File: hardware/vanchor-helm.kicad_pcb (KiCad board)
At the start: 2 copper layers, 200 x 150 mm, 113 parts, among them J1 PI_40PIN_STACK, J10 DISP PWR 5V, J11 AS5600, J12 PICO UTIL, J16 LOGIC 12-48V, J17 12V_LINK, J18 LUG BATT+, J19 LUG MOTOR A, J2 PI_BREAKOUT, J20 LUG MOTOR B, J21 LUG GND, J22 SERVO MOTOR, J3 UART0 ttyAMA0, J4 UART2 ttyAMA2, J5 UART3 ttyAMA3, J6 UART4 ttyAMA4, J7 UART5 ttyAMA5, J8 I2C1 spare, J9 FAN 5V, Q1 IRF9540N, Q10 IRF100P219, Q3 IRF100P219, Q4 IRF100P219, Q5 IRF100P219, Q6 IRF100P219, Q7 IRF100P219, Q8 IRF100P219, Q9 IRF100P219, U1 Pico 2, U10 ACS758LCB-100B, U5 D36V50F5, U6 D36V50F12, U7 BTN8982TA, U8 BTN8982TA, U9 HIP4082IPZ

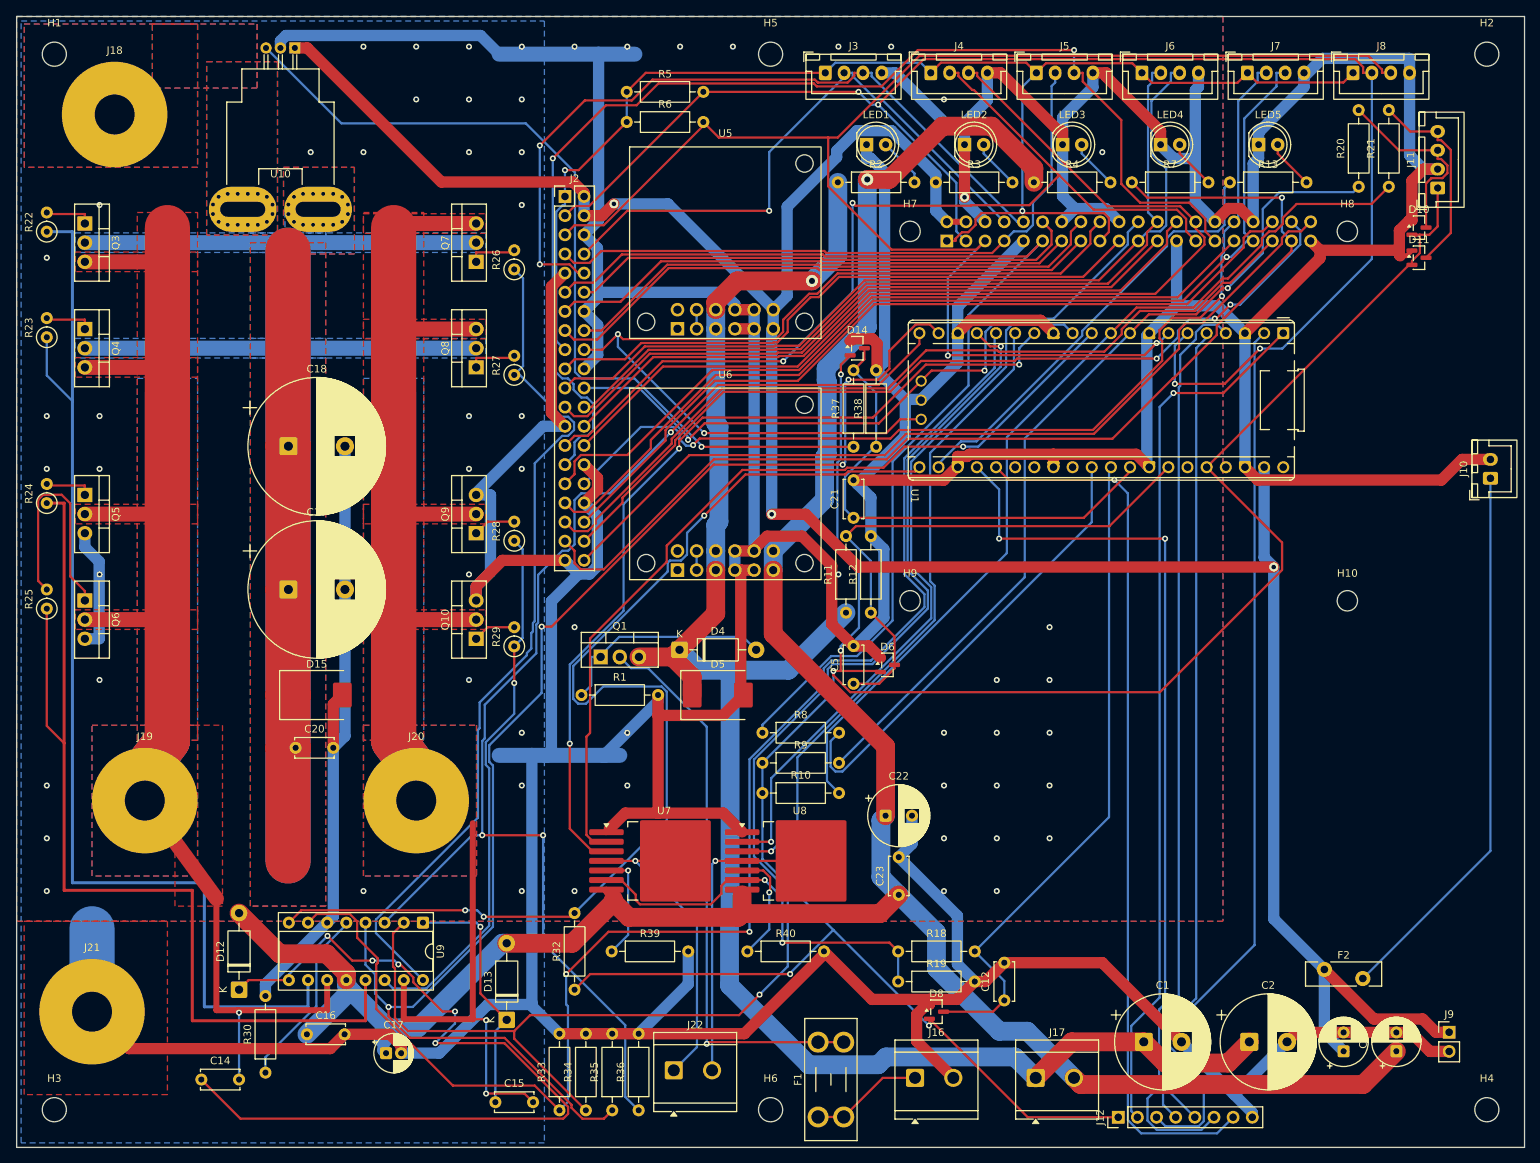
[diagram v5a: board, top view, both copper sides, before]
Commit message: cost passes 5-9: audits + cost-driver analysis + variant notes (docs/cost-optimization-log.md); v3 board script 150x120
Co-Authored-By: Claude Fable 5 <noreply@anthropic.com>
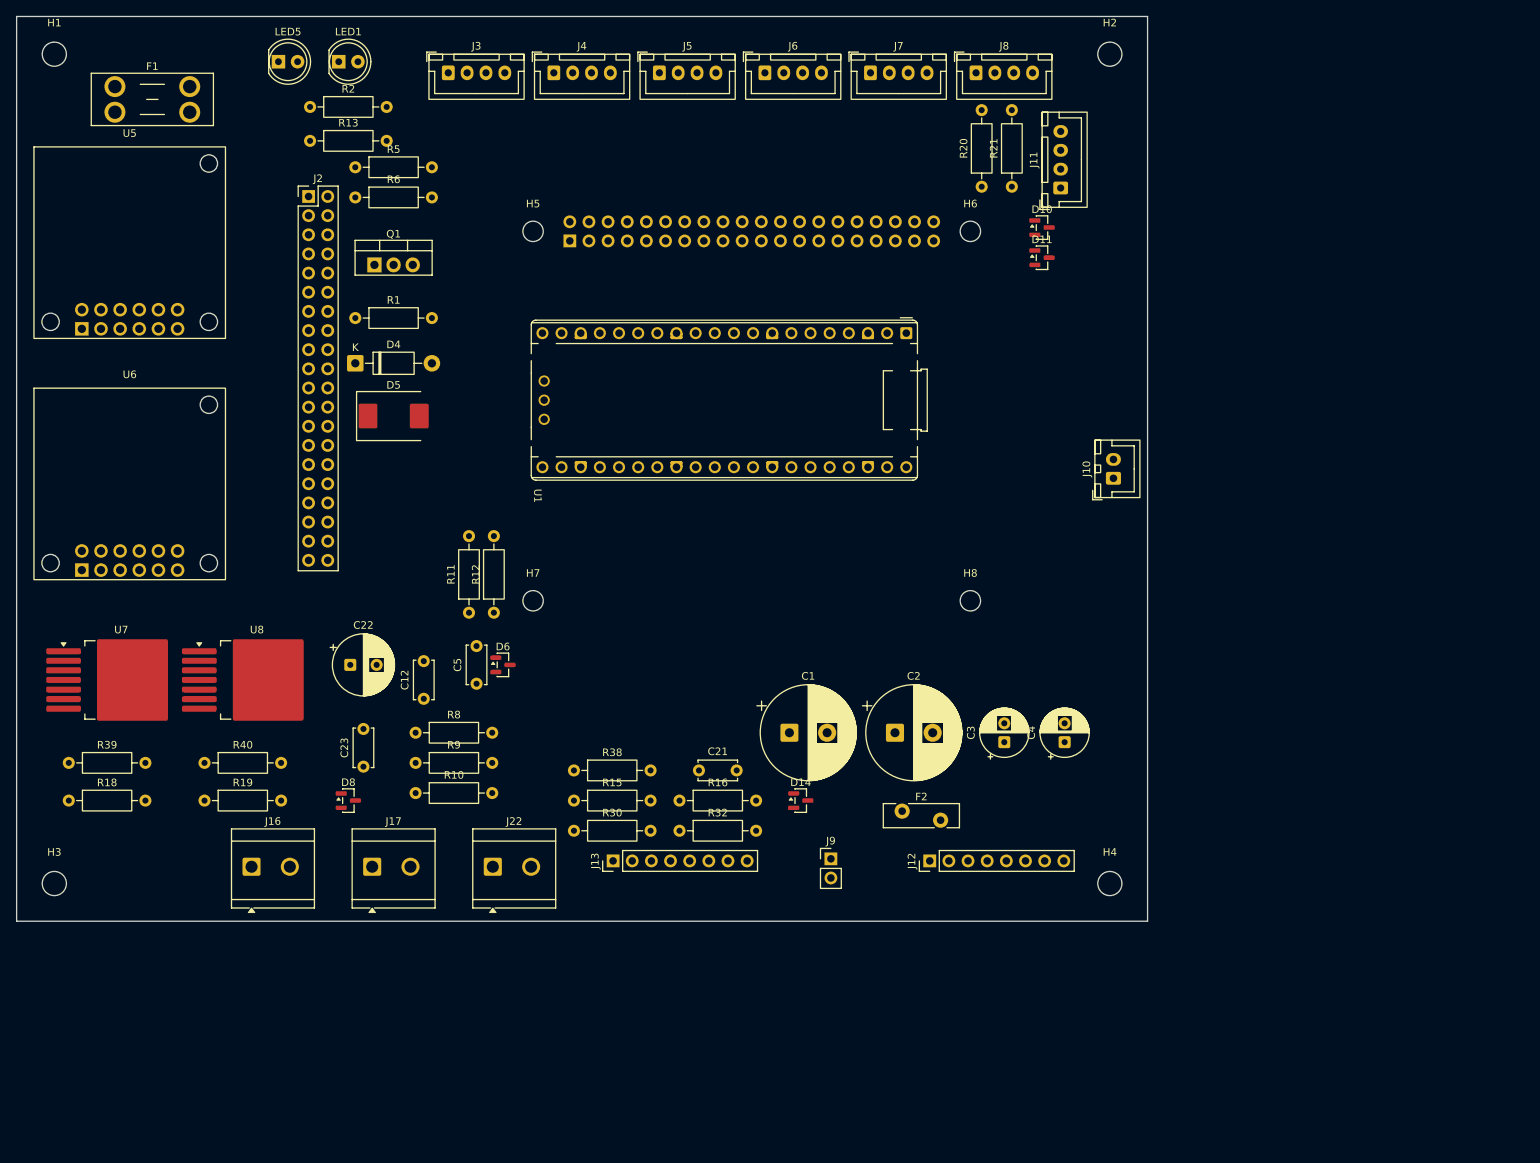
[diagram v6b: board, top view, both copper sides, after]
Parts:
- removed C14, C15: 1u/50V, C_Disc_D5.0mm_W2.5mm_P5.00mm
- removed C16: 100n, C_Disc_D5.0mm_W2.5mm_P5.00mm
- removed C17: 10u/25V, CP_Radial_D5.0mm_P2.00mm
- removed C18, C19: 2200u/63V, CP_Radial_D18.0mm_P7.50mm
- removed C20: 1u/100V film, C_Disc_D5.0mm_W2.5mm_P5.00mm
- removed D12, D13: UF4007, D_DO-41_SOD81_P10.16mm_Horizontal
- removed D15: SMCJ58A, D_SMC
- removed H10, H9: MountingHole_2.7mm_M2.5, MountingHole_2.7mm_M2.5
- removed J18: LUG BATT+, Lug_M5
- removed J19: LUG MOTOR A, Lug_M5
- removed J20: LUG MOTOR B, Lug_M5
- removed J21: LUG GND, Lug_M5
- removed LED2, LED3, LED4: green, LED_D5.0mm
- removed Q10, Q3, Q4, Q5, Q6, Q7, Q8, Q9: IRF100P219, TO-220-3_Vertical
- removed R22, R23, R24, R25, R26, R27, R28, R29: 10R, R_Axial_DIN0207_L6.3mm_D2.5mm_P2.54mm_Vertical
- removed R3, R7: 1k, R_Axial_DIN0207_L6.3mm_D2.5mm_P10.16mm_Horizontal
- removed R33, R34, R35, R36: 100k, R_Axial_DIN0207_L6.3mm_D2.5mm_P10.16mm_Horizontal
- removed R37: 10k, R_Axial_DIN0207_L6.3mm_D2.5mm_P10.16mm_Horizontal
- removed R4: 4.7k, R_Axial_DIN0207_L6.3mm_D2.5mm_P10.16mm_Horizontal
- removed U10: ACS758LCB-100B, Allegro_CB_PFF
- removed U9: HIP4082IPZ, DIP-16_W7.62mm_Socket
- added J13: THRUST DRV, PinHeader_1x08_P2.54mm_Vertical, F.Cu at (99.1, 132.0)
- added R15: 1k, R_Axial_DIN0207_L6.3mm_D2.5mm_P10.16mm_Horizontal, F.Cu at (93.9, 124.0)
- added R16: 1k, R_Axial_DIN0207_L6.3mm_D2.5mm_P10.16mm_Horizontal, F.Cu at (107.9, 124.0)
- H5, H6: value MountingHole_3.2mm_M3 -> MountingHole_2.7mm_M2.5; footprint MountingHole_3.2mm_M3 -> MountingHole_2.7mm_M2.5
- R30: value 150k -> 100k
- R32: value 10k -> 100k
- R39, R40: value 51k -> 47k
- moved F1 165.4 mm to (33.0, 29.3), turned to 0 degrees
- moved LED5 130.5 mm to (54.7, 26.0)
- moved R13 122.1 mm to (58.9, 36.5)
- moved H6 119.5 mm to (146.5, 48.5)
- moved R18 111.8 mm to (26.9, 124.0)
- moved R19 95.1 mm to (44.9, 124.0)
- moved J16 92.3 mm to (51.2, 132.8)
- moved J17 92.3 mm to (67.2, 132.8)
- moved C12 86.8 mm to (74.0, 110.5)
- moved J9 85.2 mm to (128.0, 131.7)
- moved D8 82.9 mm to (64.0, 124.0)
- moved U5 79.0 mm to (35.0, 50.0)
- moved U6 79.0 mm to (35.0, 82.0)
- moved R39 76.2 mm to (26.9, 119.0)
- moved R40 76.2 mm to (44.9, 119.0)
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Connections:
- J1 pad 37: PI_LED -> unconnected-(J1-Pin_37-Pad37)
- J2 pad 37: PI_LED -> unconnected-(J2-Pin_37-Pad37)
- R30 pad 1: /thrust/DEL -> THR_R_EN
- R32 pad 1: +3V3 -> THR_L_EN
- R32 pad 2: THR_DIS -> GND
- U1 pad 16: THR_AHI -> THR_RPWM
- U1 pad 17: THR_BHI -> THR_LPWM
- U1 pad 19: THR_ALI -> THR_R_EN
- U1 pad 20: THR_BLI -> THR_L_EN
- U1 pad 21: THR_DIS -> unconnected-(U1-GPIO16-Pad21)
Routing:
- net GND: track 1302.9 -> 0.00 mm, vias 61 -> 0
- net +12V: track 338.8 -> 0.00 mm, vias 1 -> 0
- net +5V: track 330.1 -> 0.00 mm, vias 3 -> 0
- net +3V3: track 317.4 -> 0.00 mm, vias 5 -> 0
- net VBRIDGE: track 267.3 -> 0.00 mm
- net VIN: track 236.2 -> 0.00 mm, vias 1 -> 0
- net MOTOR_A: track 234.7 -> 0.00 mm, vias 1 -> 0
- net MOTOR_B: track 234.4 -> 0.00 mm, vias 2 -> 0
- net PI_SDA: track 206.2 -> 0.00 mm, vias 4 -> 0
- net PI_SCL: track 201.5 -> 0.00 mm, vias 2 -> 0
- net THR_AHI: track 193.6 -> 0.00 mm, vias 2 -> 0
- net THR_BHI: track 191.0 -> 0.00 mm, vias 2 -> 0
- net 3V3_PI: track 189.4 -> 0.00 mm, vias 2 -> 0
- net THR_ALI: track 188.1 -> 0.00 mm, vias 4 -> 0
- net THR_BLI: track 173.3 -> 0.00 mm, vias 3 -> 0
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- removed copper zone on B.Cu, net GND
- removed copper zone on F.Cu, net GND
- removed copper zone on B.Cu, net MOTOR_A
- removed copper zone on F.Cu, net MOTOR_A
- removed copper zone on B.Cu, net MOTOR_B
- removed copper zone on F.Cu, net MOTOR_B
- removed copper zone on B.Cu, net VBAT_PWR
- removed copper zone on F.Cu, net VBAT_PWR
- removed copper zone on B.Cu, net VBRIDGE
- removed copper zone on F.Cu, net VBRIDGE
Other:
- board size 200 x 150 mm -> 150 x 120 mm

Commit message: feat: v3 cost-optimized board (pass 10) — 150x120 1oz, external thrust driver on J13, DRC clean
Co-Authored-By: Claude Fable 5 <noreply@anthropic.com>
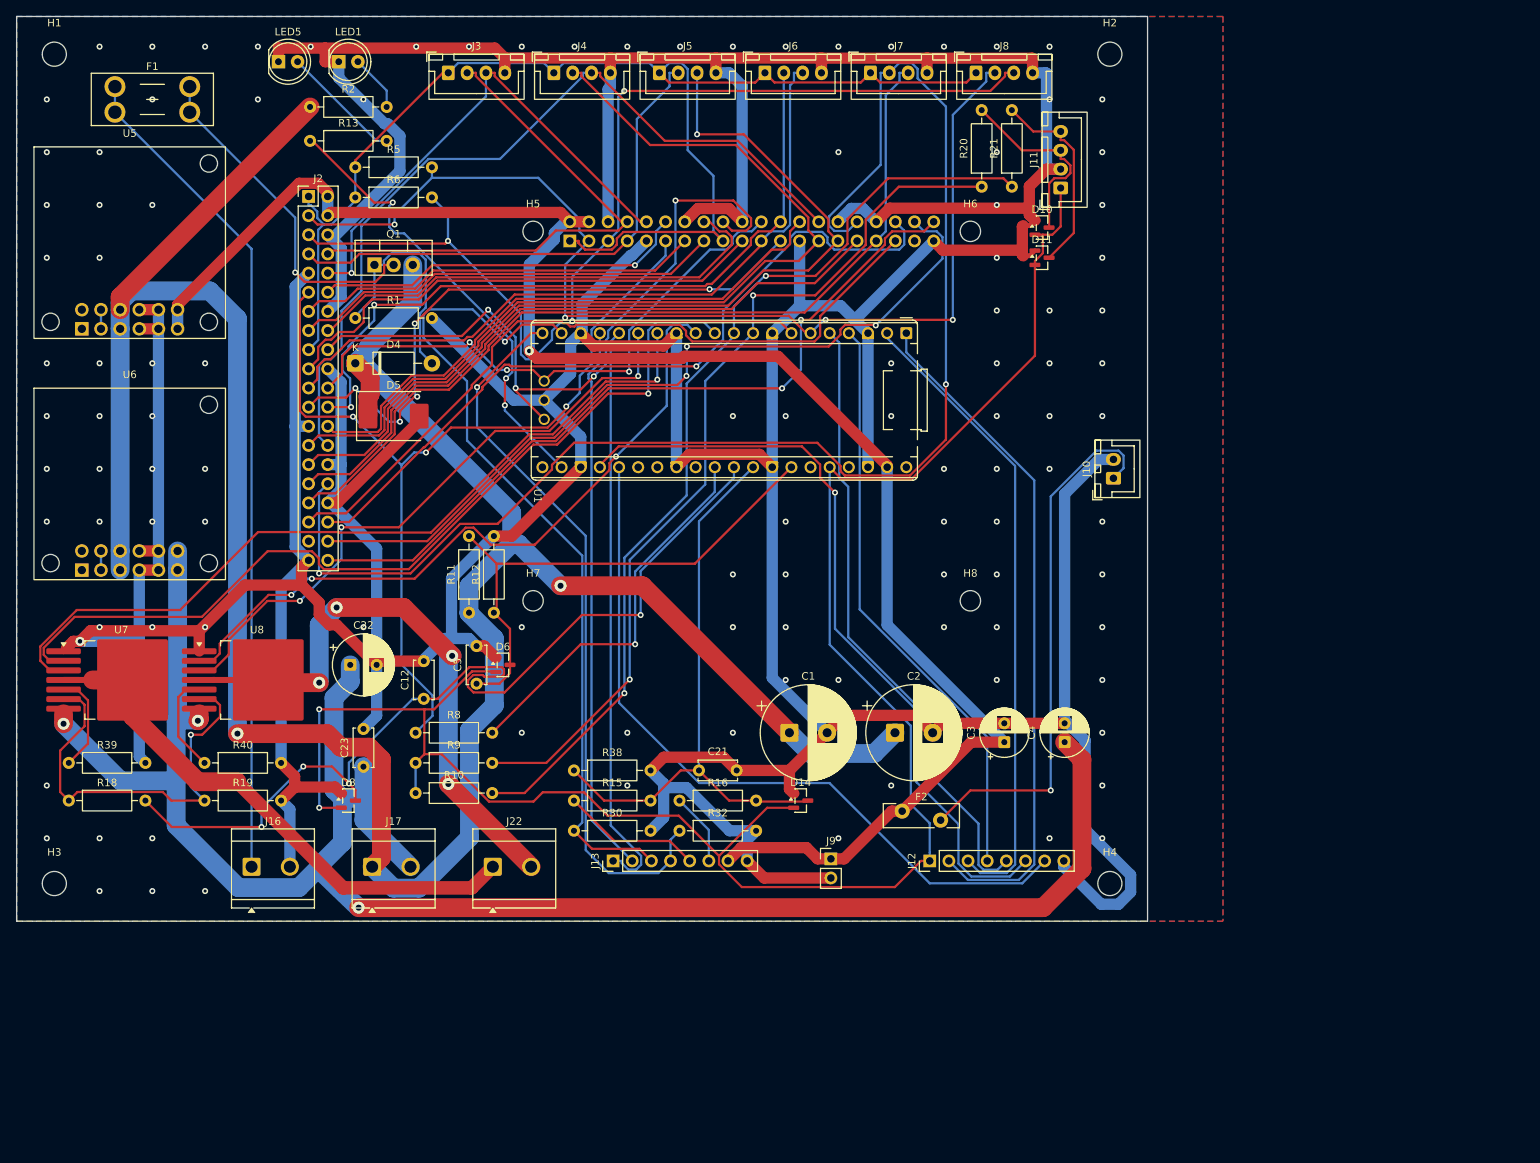
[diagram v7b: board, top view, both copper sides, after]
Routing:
- net GND: track 0.00 -> 1032.5 mm, vias 0 -> 110
- net VIN: track 0.00 -> 362.5 mm, vias 0 -> 2
- net +3V3: track 0.00 -> 260.9 mm, vias 0 -> 2
- net +12V: track 0.00 -> 256.0 mm, vias 0 -> 3
- net +5V: track 0.00 -> 229.9 mm, vias 0 -> 1
- net UART5_TX: track 0.00 -> 191.3 mm, vias 0 -> 2
- net 3V3_PI: track 0.00 -> 177.7 mm
- net PI_SCL: track 0.00 -> 170.7 mm, vias 0 -> 3
- net PI_SDA: track 0.00 -> 147.2 mm, vias 0 -> 4
- net ENC_SCL: track 0.00 -> 126.6 mm, vias 0 -> 2
- net SERVO_IS: track 0.00 -> 124.5 mm, vias 0 -> 4
- net UART2_TX: track 0.00 -> 124.1 mm
- net PI_PICO_RUN: track 0.00 -> 123.5 mm, vias 0 -> 3
- net RPWM: track 0.00 -> 118.8 mm, vias 0 -> 1
- net ENC_SDA: track 0.00 -> 118.8 mm, vias 0 -> 2
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- added copper zone on B.Cu, net GND
- added copper zone on F.Cu, net GND

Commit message: feat: v3.1 12V-only — generic 5V buck module on J14, U5/U6/J17 removed, SMCJ18A TVS, servo direct on VIN; DRC clean
Co-Authored-By: Claude Fable 5 <noreply@anthropic.com>
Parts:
- removed C4: 100u/25V, CP_Radial_D6.3mm_P2.50mm
- removed J17: 12V_LINK, TerminalBlock_CUI_TB007-508-02_1x02_P5.08mm_Horizontal
- removed U5: D36V50F5, Pololu_D36V50Fx
- removed U6: D36V50F12, Pololu_D36V50Fx
- added H10: MountingHole_2.7mm_M2.5, MountingHole_2.7mm_M2.5, F.Cu at (146.5, 97.5)
- added H9: MountingHole_2.7mm_M2.5, MountingHole_2.7mm_M2.5, F.Cu at (88.5, 97.5)
- added J14: BUCK 5V, PinHeader_1x04_P2.54mm_Vertical, F.Cu at (24.2, 50.0)
- C1, C2: value 470u/63V -> 470u/25V
- D5: value SMCJ58A -> SMCJ18A
- H5, H6: value MountingHole_2.7mm_M2.5 -> MountingHole_3.2mm_M3; footprint MountingHole_2.7mm_M2.5 -> MountingHole_3.2mm_M3
- J16: value LOGIC 12-48V -> BATT 12V
- R11: value 100k -> 47k
- R12: value 6.8k -> 10k
- R2: value 15k/0.5W -> 2.2k
- moved H4 138.0 mm to (36.0, 86.0)
- moved H5 107.3 mm to (25.0, 135.0)
- moved H6 88.5 mm to (165.0, 135.0)
- moved H3 70.9 mm to (36.0, 65.0)
- moved H7 49.0 mm to (88.5, 48.5)
- moved H8 49.0 mm to (146.5, 48.5)
- moved J22 16.0 mm to (67.2, 132.8)
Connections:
- C22 pad 1: +12V -> VIN
- C23 pad 1: +12V -> VIN
- U7 pad 7: +12V -> VIN
- U8 pad 7: +12V -> VIN
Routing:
- net +12V: track 256.0 -> 0.00 mm, vias 3 -> 0
- net GND: track 1032.5 -> 917.9 mm, vias 110 -> 118
- net +5V: track 229.9 -> 333.3 mm, vias 1 -> 0
- net UART5_TX: track 191.3 -> 112.2 mm, vias 2 -> 1
- net +3V3: track 260.9 -> 210.4 mm
- net UART2_TX: track 124.1 -> 162.0 mm
- net VIN: track 362.5 -> 329.8 mm
- net UART2_RX: track 110.2 -> 142.2 mm, vias 0 -> 1
- net PI_SDA: track 147.2 -> 177.2 mm, vias 4 -> 1
- net PI_SCL: track 170.7 -> 142.6 mm, vias 3 -> 4
- net SERVO_B: track 71.5 -> 44.3 mm, vias 4 -> 0
- net THR_LPWM: track 73.0 -> 98.7 mm
- net PI_PICO_RUN: track 123.5 -> 143.5 mm, vias 3 -> 1
- net /power/BATT_IN: track 111.0 -> 127.0 mm
- net THR_R_EN: track 111.3 -> 96.8 mm, vias 1 -> 0
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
